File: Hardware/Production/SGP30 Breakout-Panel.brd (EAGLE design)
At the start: 97.3 x 97.3 mm, 336 parts, among them J11 PTH, J14 PTH, J17 PTH, J20 PTH, J23 PTH, J26 PTH, J3 PTH, J5 PTH, J8 PTH, U1 SGP30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

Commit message: fixed missing ground connection
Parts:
- U10, U12, U14, U16, U18, U2, U4, U6, U8: value MIC5504 -> AP2112k
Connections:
- removed net N$10: U10.2
- removed net N$12: U12.2
- removed net N$14: U14.2
- removed net N$16: U16.2
- removed net N$18: U18.2
- removed net N$2 (its old number): U4.2
- removed net N$5 (its old number): U6.2
- removed net N$6 (its old number): U2.2
- removed net N$8 (its old number): U8.2
- net GND: now also U2.2
- net GND1: now also U4.2
- net GND2: now also U6.2
- net GND3: now also U8.2
- net GND4: now also U10.2
- net GND5: now also U12.2
- net GND6: now also U14.2
- net GND7: now also U16.2
- net GND8: now also U18.2
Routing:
- net GND8: track 17.1 -> 18.9 mm
- net GND5: track 17.1 -> 18.9 mm
- net GND2: track 17.1 -> 18.9 mm
- net GND6: track 17.1 -> 18.9 mm
- net GND3: track 17.1 -> 18.9 mm
- net GND: track 17.1 -> 18.9 mm
- net GND7: track 17.1 -> 18.9 mm
- net GND4: track 17.1 -> 18.9 mm
- net GND1: track 17.1 -> 18.9 mm

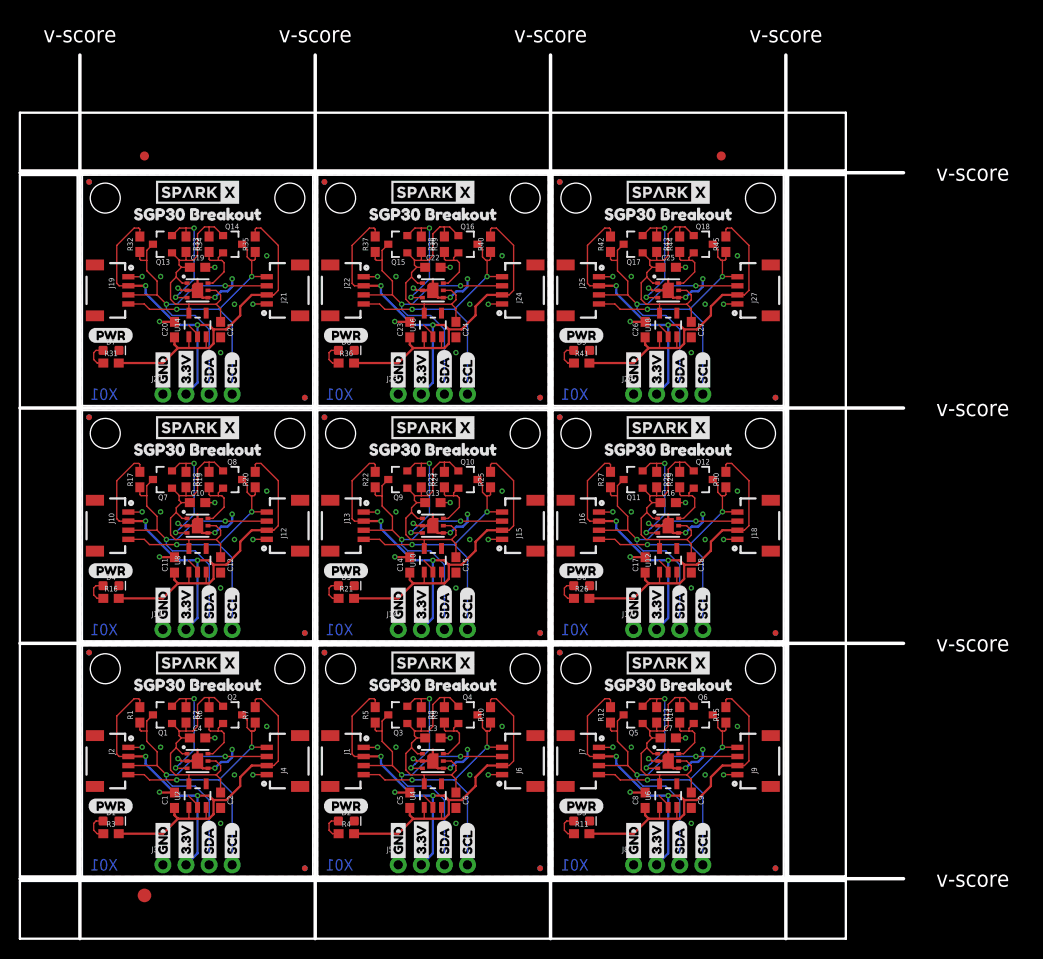
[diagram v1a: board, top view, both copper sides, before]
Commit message: Fixed ground connections
* Pad not grounded
* Connected pad to solde mask
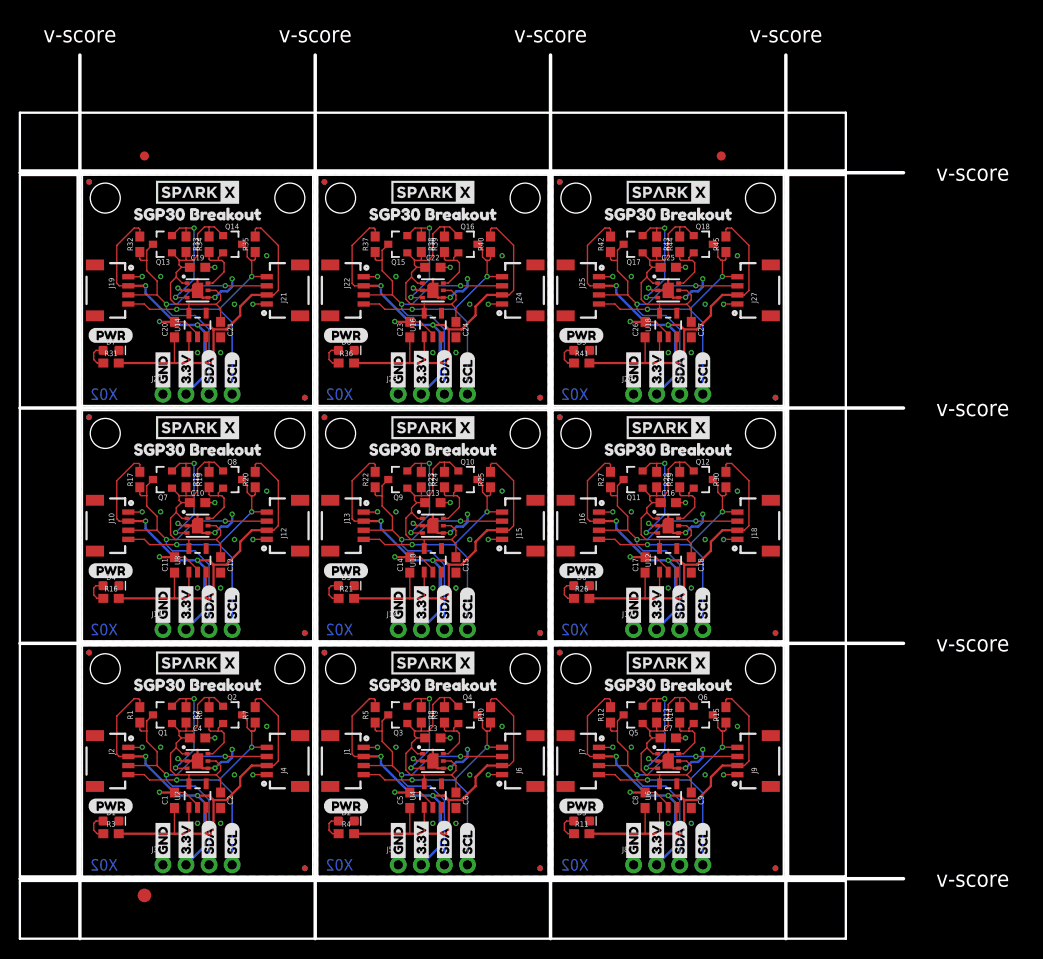
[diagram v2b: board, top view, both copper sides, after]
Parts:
- U$110, U$124, U$40, U$54, U$68, U$82, U$96: device Labels:QWIIC-LOGO-MEDIUM -> buzzard_labels (9):SGP30_BREAKOUT1
- U$112, U$126, U$42, U$56, U$70, U$84, U$98: value (none) -> QWIIC_LOGO_7MM; device buzzard_labels (9):SGP30_BREAKOUT1 -> SparkFun-Aesthetics:QWIIC_7MM
- U$12: value (none) -> SPARKX-LOGO4; device Labels-0_04:3#3V2 -> SparkX:SPARKX-MEDIUM
- U$13: device Labels-0_04:GND1 -> Labels-0_04:3#3V2
- U$14: device Labels-0_04:SCL9 -> Labels-0_04:GND1
- U$15: device Labels-0_04:SDA8 -> Labels-0_04:SCL9
- U$16: device Labels-0_04:GND1 -> Labels-0_04:SDA8
- U$17: device Labels-0_04:3#3V2 -> Labels-0_04:GND1
- U$18: device Labels-0_04:SDA8 -> Labels-0_04:3#3V2
- U$19: device Labels-0_04:SCL9 -> Labels-0_04:SDA8
- U$20: device Labels-0_04:(PWR) -> Labels-0_04:SCL9
- U$23: device Labels:QWIIC-LOGO-MEDIUM -> Labels-0_04:(PWR)
- U$28, U$9: value SPARKX-LOGO4 -> QWIIC_LOGO_7MM; device SparkX:SPARKX-MEDIUM -> SparkFun-Aesthetics:QWIIC_7MM
- U$29: value (none) -> SPARKX-LOGO4; device Labels:QWIIC-LOGO-MEDIUM -> SparkX:SPARKX-MEDIUM
- moved U$29 47.0 mm to (64.5, 23.5)
- moved U$28 26.4 mm to (38.6, 18.4)
- moved U$9 26.4 mm to (12.7, 18.4)
- moved U$40 23.9 mm to (56.4, 21.1), flipped to the top
- moved U$82 23.9 mm to (56.4, 47.0), flipped to the top
- moved U$124 23.9 mm to (56.4, 72.9), flipped to the top
- moved U$54 23.9 mm to (4.57, 47.0), flipped to the top
- moved U$68 23.9 mm to (30.5, 47.0), flipped to the top
- moved U$110 23.9 mm to (30.5, 72.9), flipped to the top
- moved U$96 23.9 mm to (4.57, 72.9), flipped to the top
- moved U$12 22.0 mm to (38.6, 23.5), turned to 0 degrees
- moved U$23 21.2 mm to (26.5, 7.75), flipped to the top
- moved U$20 17.1 mm to (42.4, 1.52), flipped to the bottom, turned to 90 degrees
- moved U$125 16.3 mm to (72.6, 72.9), flipped to the bottom
- moved U$41 16.3 mm to (72.6, 21.1), flipped to the bottom
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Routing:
- net 3.3V5: track 68.6 -> 71.7 mm
- net 3.3V4: track 68.6 -> 71.7 mm
- net 3.3V3: track 68.6 -> 71.7 mm
- net 3.3V8: track 68.6 -> 71.7 mm
- net 3.3V7: track 68.6 -> 71.7 mm
- net 3.3V2: track 68.6 -> 71.7 mm
- net 3.3V1: track 68.6 -> 71.7 mm
- net 3.3V: track 68.6 -> 71.7 mm
- net 3.3V6: track 68.6 -> 71.7 mm
- net GND8: track 18.9 -> 20.5 mm, vias 11 -> 12
- net GND7: track 18.9 -> 20.5 mm, vias 11 -> 12
- net GND6: track 18.9 -> 20.5 mm, vias 11 -> 12
- net GND5: track 18.9 -> 20.5 mm, vias 11 -> 12
- net GND4: track 18.9 -> 20.5 mm, vias 11 -> 12
- net GND3: track 18.9 -> 20.5 mm, vias 11 -> 12
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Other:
- board text added: "X02"
- board text removed: "X01"
